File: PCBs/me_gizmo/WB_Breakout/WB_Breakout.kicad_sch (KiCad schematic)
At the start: 36 parts, among them J1 Conn_01x06_Pin, J2 Conn_01x24_Pin, J3 Conn_01x09_Pin, U1 ADG714, U2 ADG714, U3 ADG714, U4 ADG714, U5 XS3A4053, U6 XS3A4053

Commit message: Completed ADG714 Breakout kicad (awaiting further review)
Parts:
- removed J1: Conn_01x06_Pin, Connector_PinHeader_1.00mm:PinHeader_1x06_P1.00mm_Vertical, symbol Connector:Conn_01x06_Pin
- removed J2: Conn_01x24_Pin, Connector_PinHeader_1.00mm:PinHeader_1x24_P1.00mm_Vertical, symbol Connector:Conn_01x24_Pin
- removed J3: Conn_01x09_Pin, Connector_PinHeader_1.00mm:PinHeader_1x09_P1.00mm_Vertical, symbol Connector:Conn_01x09_Pin
- removed U5, U6: XS3A4053, Multiplexer:TSSOP-16, symbol Multiplexer:74HC4053
- added J1: Conn_01x08_Pin, Connector_PinHeader_2.54mm:PinHeader_1x08_P2.54mm_Vertical, symbol Connector:Conn_01x08_Pin
- added J2: Conn_01x05_Pin, Connector_PinHeader_2.54mm:PinHeader_1x05_P2.54mm_Vertical, symbol Connector:Conn_01x05_Pin
- added J4: Conn_01x10_Pin, Connector_PinHeader_2.54mm:PinHeader_1x10_P2.54mm_Vertical, symbol Connector:Conn_01x10_Pin
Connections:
- net 2ADC_IN1+ is gone; now on net RE2: U3.19 (D8)
- net 2ADC_IN1- is gone; now on net RD2: U3.17 (D7)
- net 2ADC_IN2+ is gone; now on net RB2: U3.15 (D6)
- net 2ADC_IN2- is gone; now on net RA2: U3.13 (D5)
- net 2ADC_IN3+ is gone; now on net RA1: U3.12 (D4)
- net 2ADC_IN3- is gone; now on net RB1: U3.10 (D3)
- net 2ADC_IN4+ is gone; now on net RD1: U3.8 (D2)
- net 2ADC_IN4- is gone; now on net RE1: U3.6 (D1)
- net 2.5V: now also U2.10 (D3), U2.12 (D4), U2.14 (S5), U2.16 (S6), U2.18 (S7), U2.20 (S8), U2.6 (D1), U2.8 (D2), J4.1 (Pin_1); no longer U1.16 (S6), U1.9 (S3), U2.11 (S4), U2.5 (S1)
- net CIPO: now also J2.5 (Pin_5)
- net CS: now also J2.4 (Pin_4)
- net GND: now also J4.10 (Pin_10)
- net HB_OUT1+: now also U1.11 (S4), U3.11 (S4), U3.14 (S5), J1.8 (Pin_8); no longer U1.5 (S1), U3.20 (S8)
- net HB_OUT1-: now also U1.9 (S3), U3.16 (S6), U3.9 (S3), J1.7 (Pin_7); no longer U1.7 (S2), U3.18 (S7)
- net HB_OUT2+: now also U1.7 (S2), U3.18 (S7), U3.7 (S2), J1.6 (Pin_6); no longer U1.11 (S4), U3.16 (S6)
- net HB_OUT2-: now also U1.5 (S1), U3.20 (S8), U3.5 (S1), J1.5 (Pin_5); no longer U1.14 (S5), U3.14 (S5)
- net HB_OUT3+: now also U1.20 (S8), U4.11 (S4), U4.14 (S5), J1.4 (Pin_4); no longer U1.18 (S7), U3.11 (S4)
- net HB_OUT3-: now also U1.18 (S7), U4.16 (S6), U4.9 (S3), J1.3 (Pin_3); no longer U1.20 (S8), U3.9 (S3)
- net HB_OUT4+: now also U1.16 (S6), U4.18 (S7), U4.7 (S2), J1.2 (Pin_2); no longer U2.7 (S2), U3.7 (S2)
- net HB_OUT4-: now also U1.14 (S5), U4.20 (S8), U4.5 (S1), J1.1 (Pin_1); no longer U2.9 (S3), U3.5 (S1)
- net RC1: now also U2.13 (D5)
- net RC2: now also U2.15 (D6)
- net RESET: now also J2.3 (Pin_3)
- net RF1: now also U2.17 (D7)
- net RF2: now also U2.19 (D8)
- net RG1: now also U4.12 (D4); no longer U4.6 (D1)
- net RG2: now also U4.13 (D5); no longer U4.10 (D3)
- net RH1: now also U4.10 (D3); no longer U4.8 (D2)
- net RH2: now also U4.15 (D6); no longer U4.12 (D4)
- net RI1: now also R19.1, U2.5 (S1); no longer U2.13 (D5)
- net RI2: now also R23.1, U2.7 (S2); no longer U4.13 (D5)
- net RJ1: now also U4.8 (D2); no longer U2.15 (D6)
- net RJ2: now also U4.17 (D7); no longer U4.15 (D6)
- net RK1: now also U4.6 (D1); no longer U2.17 (D7)
- net RK2: now also U4.19 (D8); no longer U4.17 (D7)
- net RL1: now also U2.9 (S3); no longer U2.19 (D8)
- net RL2: now also U2.11 (S4); no longer U4.19 (D8)
- net SCLK: now also J2.2 (Pin_2)
- net VDD: now also J2.1 (Pin_1)
- net branch1 renamed ADC_IN2-
- net ADC_IN2-: now also J4.5 (Pin_5)
- removed net branch10: U2.16 (S6), U2.8 (D2), U4.16 (S6)
- removed net branch11: U2.10 (D3), U2.18 (S7), U4.18 (S7)
- removed net branch12: U2.12 (D4), U2.20 (S8), U4.20 (S8)
- net branch2 renamed ADC_IN2+
- net ADC_IN2+: now also J4.4 (Pin_4)
- net branch3 renamed ADC_IN1-
- net ADC_IN1-: now also J4.3 (Pin_3)
- net branch4 renamed ADC_IN1+
- net ADC_IN1+: now also J4.2 (Pin_2)
- net branch5 renamed ADC_IN4-
- net ADC_IN4-: now also J4.9 (Pin_9)
- net branch6 renamed ADC_IN4+
- net ADC_IN4+: now also J4.8 (Pin_8)
- removed net branch7: U1.17 (D7), U4.5 (S1), U4.9 (S3)
- removed net branch8: U1.19 (D8), U4.11 (S4), U4.7 (S2)
- removed net branch9: U2.14 (S5), U2.6 (D1), U4.14 (S5)
- new net ADC_IN3+: J4.6 (Pin_6), U1.19 (D8)
- new net ADC_IN3-: J4.7 (Pin_7), U1.17 (D7)
- no-connect marks 2 -> 1
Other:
- moved on the sheet: R1, R19, R2, R20, R21, R22, R23, R24, R25, R26, R27, R28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

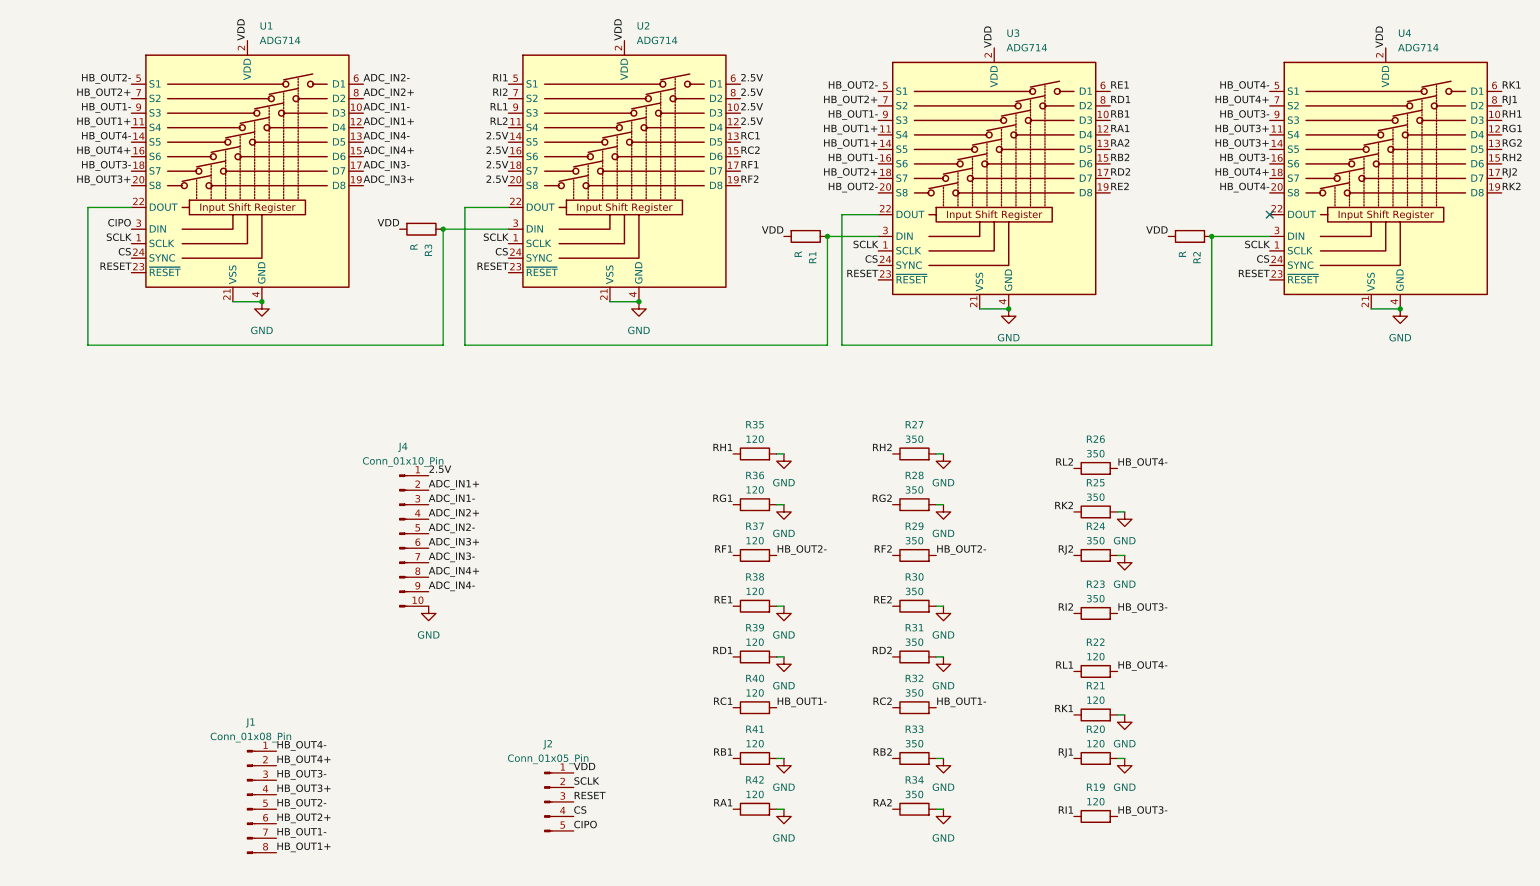
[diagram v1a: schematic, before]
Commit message: Updated resistor values in schematic, moved vias off pads, added bypass capacitors
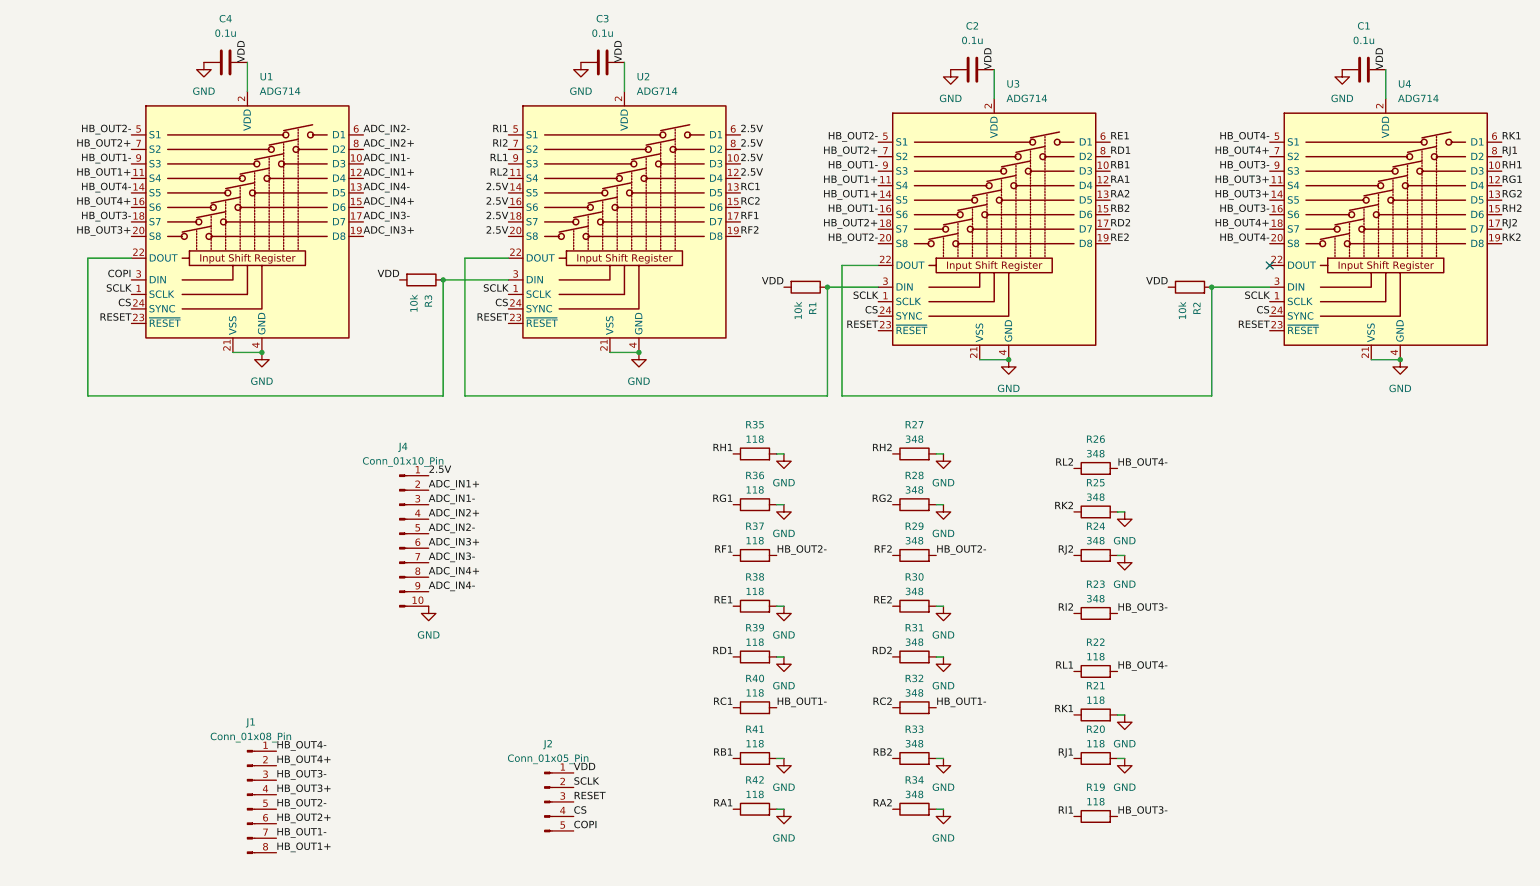
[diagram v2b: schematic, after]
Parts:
- added C1, C2, C3, C4: 0.1u, Capacitor_SMD:C_0603_1608Metric, symbol Device:C
- R1, R2, R3: value R -> 10k
- R19, R20, R21, R22, R35, R36, R37, R38, R39, R40, R41, R42: value 120 -> 118
- R23, R24, R25, R26, R27, R28, R29, R30, R31, R32, R33, R34: value 350 -> 348
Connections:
- net GND: now also C1.1, C2.1, C3.1, C4.1
- net VDD: now also C1.2, C2.2, C3.2, C4.2
- net CIPO renamed COPI
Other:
- moved on the sheet: R1, R2, R3, U1, U2, U3, U4
